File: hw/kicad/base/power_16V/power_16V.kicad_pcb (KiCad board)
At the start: 2 copper layers, 45 x 45 mm, 33 parts, among them J1 USB_B_Micro, J3 TOP, J4 BUTTOM, U1 LM2596S-5, U2 LM1117MP-3.3, U3 CP2104

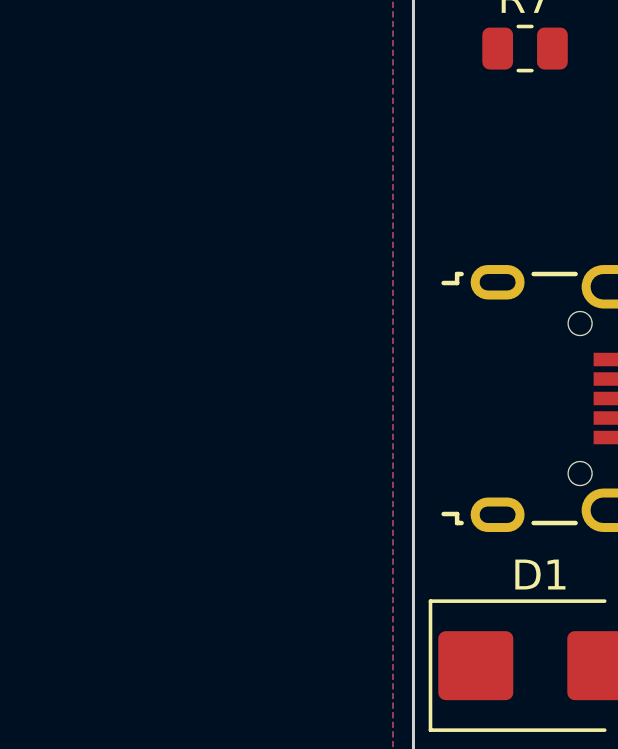
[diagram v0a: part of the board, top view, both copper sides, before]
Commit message: 增加电流传感器芯片
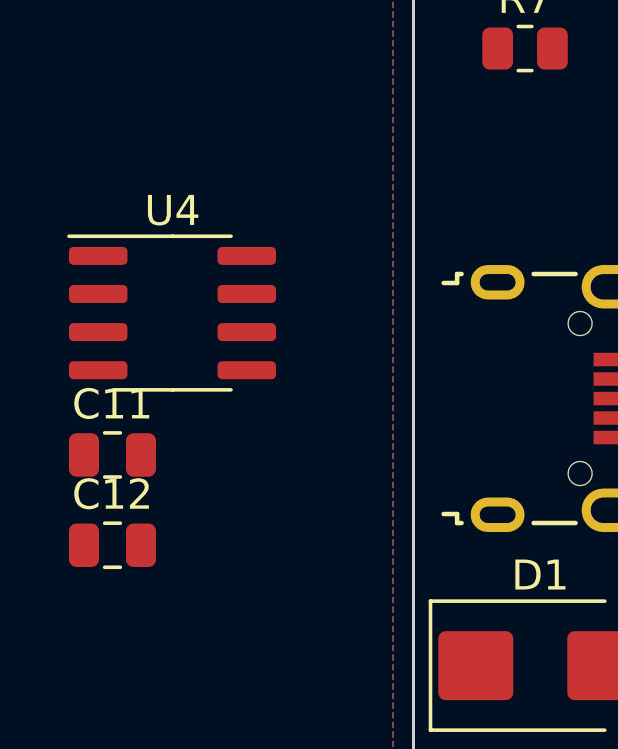
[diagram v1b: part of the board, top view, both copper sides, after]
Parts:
- added C11: 0.1uF, Capacitor_SMD:C_0805_2012Metric, F.Cu at (40.7, 61.1)
- added C12: 0.1uF, Capacitor_SMD:C_0805_2012Metric, F.Cu at (40.7, 64.1)
- added U4: ACS712xLCTR-05B, Package_SO:SOIC-8_3.9x4.9mm_P1.27mm, F.Cu at (42.7, 56.4)
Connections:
- net Net-(D6-A) renamed /DCDC_+5V
- C10 pad 1: +BATT -> Net-(J2-+)

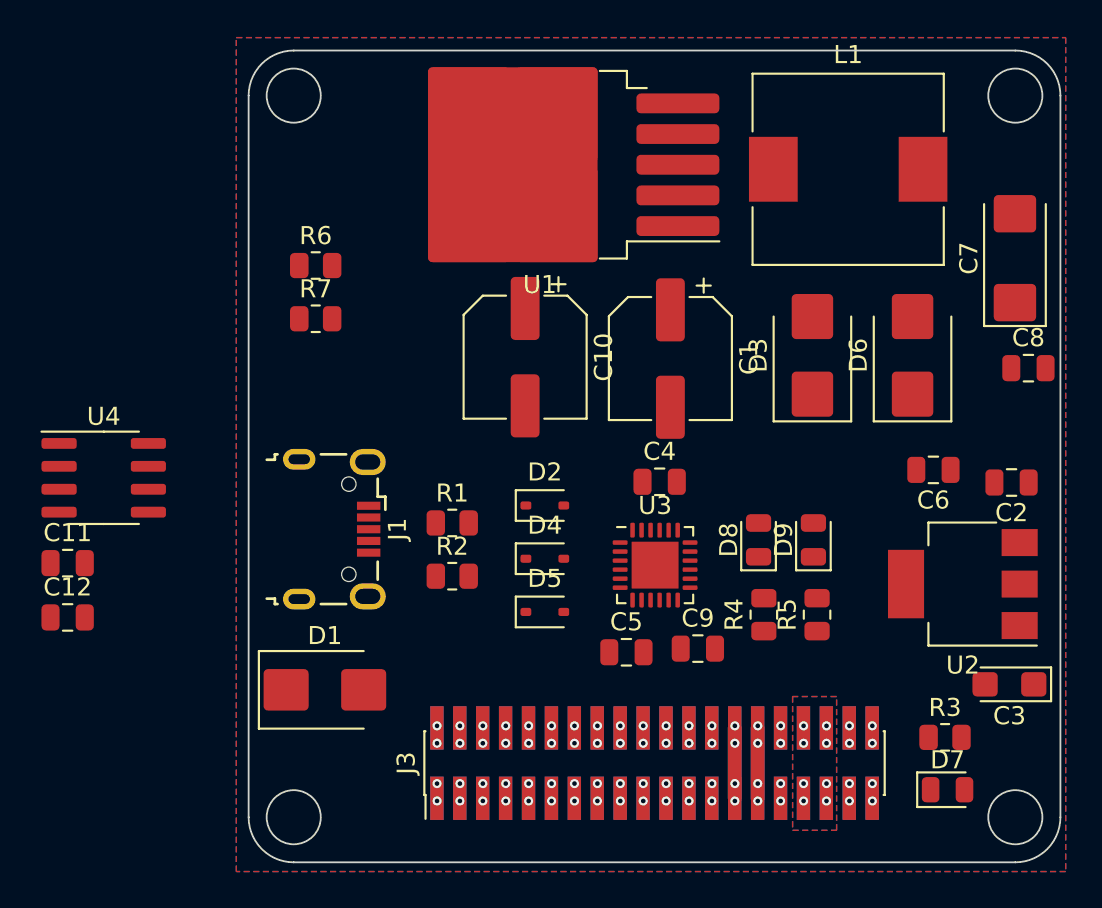
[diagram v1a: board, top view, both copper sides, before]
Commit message: 更新power16V板
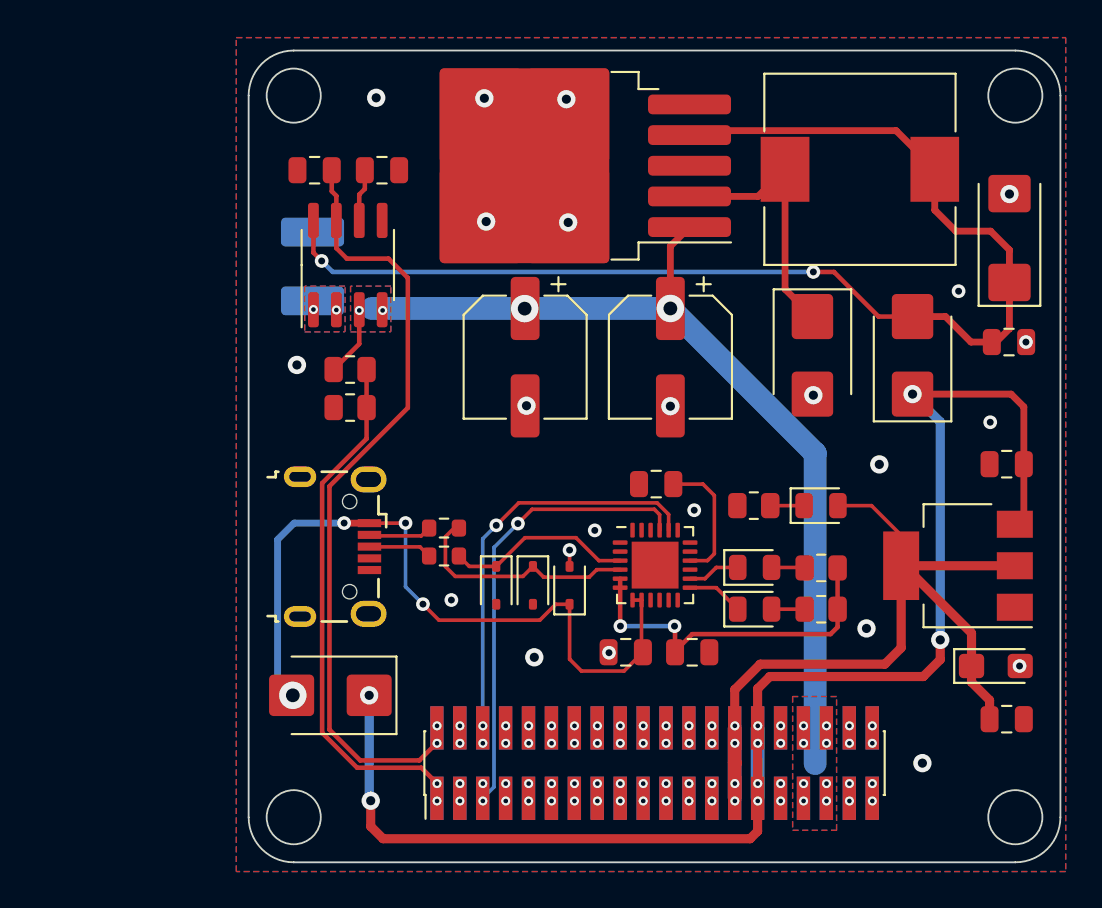
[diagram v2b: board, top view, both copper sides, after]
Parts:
- added ?: , , B.Cu at (54.3, 46.6)
- added ?: , , B.Cu at (54.3, 42.8)
- R1, R2: footprint Resistor_SMD:R_0805_2012Metric -> Resistor_SMD:R_0603_1608Metric
- R4, R5: value 22 -> 100
- moved C12 28.3 mm to (54.4, 39.4), turned to 180 degrees
- moved C11 27.9 mm to (58.1, 39.4)
- moved U4 17.9 mm to (56.2, 44.6), turned to 90 degrees
- moved D7 17.2 mm to (82.4, 57.9)
- moved R3 16.7 mm to (78.7, 57.9)
- moved C6 14.4 mm to (92.7, 69.8), turned to 0 degrees
- moved R6 6.07 mm to (56.3, 50.4)
- moved R7 5.28 mm to (56.3, 52.5), turned to 180 degrees
- moved D2 4.63 mm to (68.5, 62.4), turned to 90 degrees
- moved D8 3.85 mm to (78.8, 63.7), turned to 0 degrees
- moved D9 3.60 mm to (78.8, 61.4), turned to 0 degrees
- moved R4 3.19 mm to (82.5, 63.7), turned to 0 degrees
- moved D5 3.07 mm to (64.4, 62.4), turned to -90 degrees
- moved R2 2.71 mm to (61.6, 59.2)
- moved R5 2.60 mm to (82.5, 61.4), turned to 0 degrees
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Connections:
- C10 pad 1: Net-(J2-+) -> +BATT
- U4 pad 1: Net-(J2-+) -> /+BATT_IN
- U4 pad 2: Net-(J2-+) -> /+BATT_IN
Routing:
- net +5V: track 7.80 -> 82.5 mm, vias 4 -> 8
- net /DCDC_+5V: track 0.00 -> 69.0 mm, vias 0 -> 2
- net +BATT: track 0.00 -> 54.2 mm, vias 8 -> 12
- net /ADC_2: track 0.00 -> 43.8 mm
- net +3.3V: track 7.80 -> 49.4 mm
- net Net-(D1-A): track 0.00 -> 41.5 mm, vias 0 -> 4
- net /ADC_1: track 0.00 -> 29.5 mm
- net /UART1_Rx: track 0.00 -> 25.2 mm, vias 2 -> 3
- net /UART1_Tx: track 0.00 -> 22.8 mm, vias 2 -> 3
- net /VIO: track 0.00 -> 20.0 mm, vias 0 -> 2
- net Net-(D3-K): track 0.00 -> 14.7 mm
- net Net-(D4-K): track 0.00 -> 13.2 mm
- net Net-(D5-K): track 0.00 -> 10.4 mm
- net Net-(U3-VPP): track 0.00 -> 7.27 mm
- net Net-(J1-D+): track 0.00 -> 3.52 mm
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- added copper zone on B.Cu, net +BATT
- added copper zone on F.Cu, net +BATT
- added copper zone on B.Cu, net /+BATT_IN
- added copper zone on F.Cu, net /+BATT_IN
- added copper zone on B.Cu, net GND
- added copper zone on F.Cu, net GND
- removed copper zone on B.Cu, net (none)
- removed copper zone on F.Cu, net (none)
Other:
- board text added: "Pindar v1.2 (Base) power16v v1.2"

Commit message: 更新CPU板
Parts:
- moved ? 0.06 mm to (54.3, 46.6)
- moved ? 0.05 mm to (54.3, 42.8)

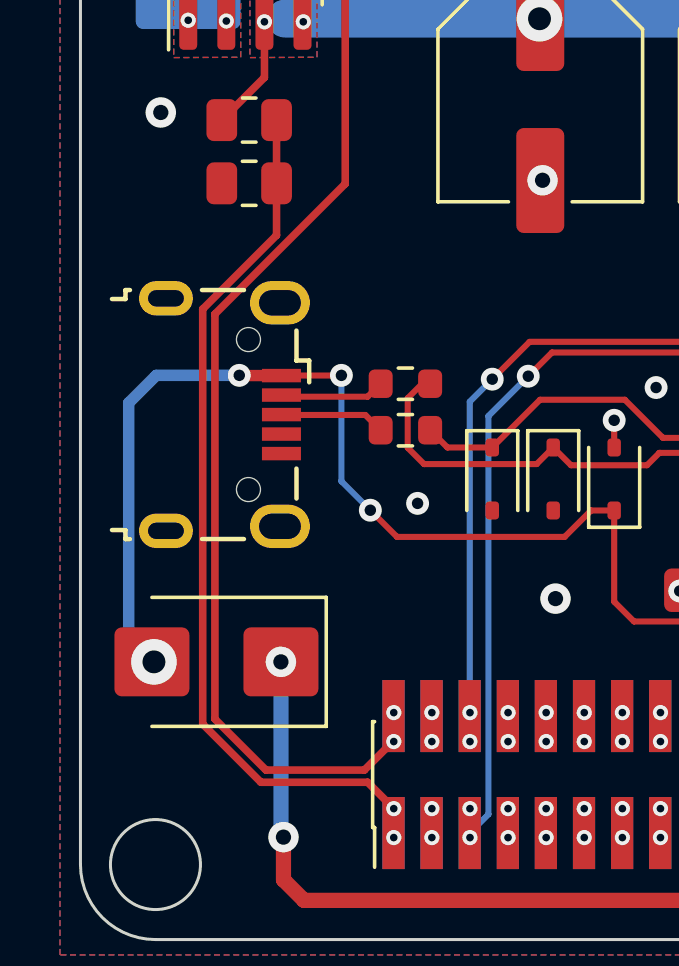
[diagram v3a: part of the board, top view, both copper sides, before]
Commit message: 更新ESP32 S3 CPU板
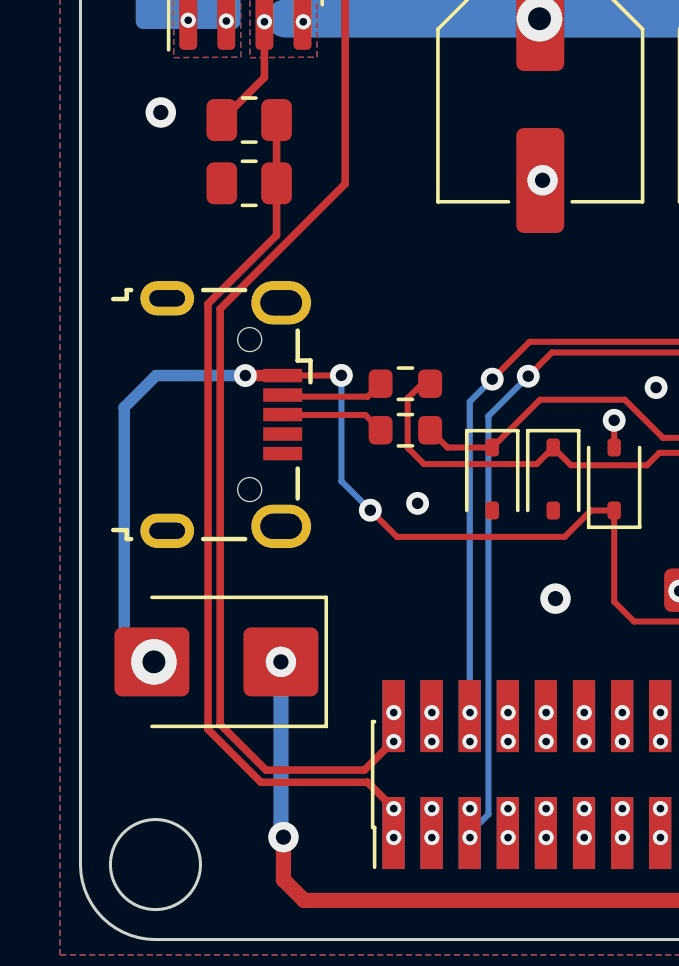
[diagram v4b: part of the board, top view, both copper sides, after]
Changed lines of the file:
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@@
   )
   (footprint "Connector_USB:USB_Micro-B_Wuerth_629105150521" (layer "F.Cu")
-    (at 55.52 60.22 -90)
+    (at 55.561 60.22 -90)
     (descr "USB Micro-B receptacle, http://www.mouser.com/ds/2/445/629105150521-469306.pdf")
     (tags "usb micro receptacle")
@@
   (via (at 75.1332 71.12) (size 0.508) (drill 0.254) (layers "F.Cu" "B.Cu") (net 13))
   (via (at 75.1332 70.1548) (size 0.508) (drill 0.254) (layers "F.Cu" "B.Cu") (net 13))
-  (segment (start 61.155 73.34) (end 60.2918 72.4768) (width 0.254) (layer "F.Cu") (net 14))
+  (segment (start 57.2567 54.2415) (end 57.2567 52.5124) (width 0.254) (layer "F.Cu") (net 14))
   (segment (start 61.155 74.17) (end 61.155 73.34) (width 0.254) (layer "F.Cu") (net 14))
   (segment (start 57.2567 50.4042) (end 57.2567 52.5124) (width 0.254) (layer "F.Cu") (net 14))
-  (segment (start 57.2567 54.2415) (end 57.2567 52.5124) (width 0.254) (layer "F.Cu") (net 14))
+  (segment (start 54.9726 70.714736) (end 54.9726 56.5256) (width 0.254) (layer "F.Cu") (net 14))
+  (segment (start 56.734664 72.4768) (end 54.9726 70.714736) (width 0.254) (layer "F.Cu") (net 14))
   (segment (start 60.2918 72.4768) (end 56.734664 72.4768) (width 0.254) (layer "F.Cu") (net 14))
-  (segment (start 54.7948 70.536936) (end 54.7948 56.7034) (width 0.254) (layer "F.Cu") (net 14))
-  (segment (start 54.7948 56.7034) (end 57.2567 54.2415) (width 0.254) (layer "F.Cu") (net 14))
-  (segment (start 56.734664 72.4768) (end 54.7948 70.536936) (width 0.254) (layer "F.Cu") (net 14))
+  (segment (start 61.155 73.34) (end 60.2918 72.4768) (width 0.254) (layer "F.Cu") (net 14))
+  (segment (start 54.9726 56.5256) (end 57.2567 54.2415) (width 0.254) (layer "F.Cu") (net 14))
   (via (at 61.1632 73.3552) (size 0.508) (drill 0.254) (layers "F.Cu" "B.Cu") (net 14))
   (via (at 61.1632 74.3204) (size 0.508) (drill 0.254) (layers "F.Cu" "B.Cu") (net 14))
@@
   (segment (start 63.695 70.27) (end 63.695 59.792) (width 0.2032) (layer "B.Cu") (net 18))
   (segment (start 63.695 59.792) (end 64.4468 59.0402) (width 0.2032) (layer "B.Cu") (net 18))
-  (segment (start 60.1846 72.0704) (end 56.903 72.0704) (width 0.254) (layer "F.Cu") (net 19))
   (segment (start 55.5822 40.7776) (end 55.3282 40.5236) (width 0.254) (layer "F.Cu") (net 19))
-  (segment (start 56.903 72.0704) (end 55.2012 70.3686) (width 0.254) (layer "F.Cu") (net 19))
-  (segment (start 55.2012 70.3686) (end 55.2012 56.871736) (width 0.254) (layer "F.Cu") (net 19))
-  (segment (start 59.5446 45.3242) (end 58.4778 44.2574) (width 0.254) (layer "F.Cu") (net 19))
-  (segment (start 55.3282 40.5236) (end 55.3282 39.3552) (width 0.254) (layer "F.Cu") (net 19))
+  (segment (start 56.903 72.0704) (end 55.379 70.5464) (width 0.254) (layer "F.Cu") (net 19))
   (segment (start 55.5822 43.6732) (end 55.5822 42.138) (width 0.254) (layer "F.Cu") (net 19))
-  (segment (start 56.1664 44.2574) (end 55.5822 43.6732) (width 0.254) (layer "F.Cu") (net 19))
+  (segment (start 61.155 71.1) (end 60.1846 72.0704) (width 0.254) (layer "F.Cu") (net 19))
   (segment (start 61.155 70.27) (end 61.155 71.1) (width 0.254) (layer "F.Cu") (net 19))
-  (segment (start 55.2012 56.871736) (end 59.5446 52.528336) (width 0.254) (layer "F.Cu") (net 19))
+  (segment (start 55.3282 40.5236) (end 55.3282 39.3552) (width 0.254) (layer "F.Cu") (net 19))
+  (segment (start 60.1846 72.0704) (end 56.903 72.0704) (width 0.254) (layer "F.Cu") (net 19))
+  (segment (start 55.379 56.693936) (end 59.5446 52.528336) (width 0.254) (layer "F.Cu") (net 19))
+  (segment (start 56.1664 44.2574) (end 55.5822 43.6732) (width 0.254) (layer "F.Cu") (net 19))
+  (segment (start 55.379 70.5464) (end 55.379 56.693936) (width 0.254) (layer "F.Cu") (net 19))
+  (segment (start 58.4778 44.2574) (end 56.1664 44.2574) (width 0.254) (layer "F.Cu") (net 19))
+  (segment (start 59.5446 45.3242) (end 58.4778 44.2574) (width 0.254) (layer "F.Cu") (net 19))
   (segment (start 55.5822 42.138) (end 55.5822 40.7776) (width 0.254) (layer "F.Cu") (net 19))
   (segment (start 59.5446 52.528336) (end 59.5446 45.3242) (width 0.254) (layer "F.Cu") (net 19))
-  (segment (start 58.4778 44.2574) (end 56.1664 44.2574) (width 0.254) (layer "F.Cu") (net 19))
-  (segment (start 61.155 71.1) (end 60.1846 72.0704) (width 0.254) (layer "F.Cu") (net 19))
   (via (at 61.1632 70.1548) (size 0.508) (drill 0.254) (layers "F.Cu" "B.Cu") (net 19))
   (via (at 61.1632 71.12) (size 0.508) (drill 0.254) (layers "F.Cu" "B.Cu") (net 19))
@@
   (segment (start 59.4176 58.9132) (end 59.4108 58.92) (width 0.2032) (layer "F.Cu") (net 32))
   (segment (start 69.1712 67.1174) (end 71.5334 67.1174) (width 0.2032) (layer "F.Cu") (net 32))
-  (segment (start 56.0208 58.92) (end 56.014 58.9132) (width 0.381) (layer "F.Cu") (net 32))
   (segment (start 67.7402 63.4176) (end 68.5108 63.4176) (width 0.2032) (layer "F.Cu") (net 32))
-  (segment (start 57.42 58.92) (end 56.0208 58.92) (width 0.381) (layer "F.Cu") (net 32))
   (segment (start 66.8598 64.298) (end 67.7402 63.4176) (width 0.2032) (layer "F.Cu") (net 32))
   (segment (start 71.5334 67.1174) (end 72.5748 66.076) (width 0.2032) (layer "F.Cu") (net 32))
   (segment (start 72.4986 63.1873) (end 72.502 63.1839) (width 0.2032) (layer "F.Cu") (net 32))
   (segment (start 60.3828 63.409) (end 61.2718 64.298) (width 0.2032) (layer "F.Cu") (net 32))
+  (segment (start 57.42 58.92) (end 56.2172 58.92) (width 0.381) (layer "F.Cu") (net 32))
   (segment (start 72.502 63.1839) (end 72.002 63.1839) (width 0.2032) (layer "F.Cu") (net 32))
   (segment (start 59.4108 58.92) (end 57.42 58.92) (width 0.2032) (layer "F.Cu") (net 32))
@@
   (via (at 59.4176 58.9132) (size 0.762) (drill 0.381) (layers "F.Cu" "B.Cu") (net 32))
   (via (at 60.3828 63.409) (size 0.762) (drill 0.381) (layers "F.Cu" "B.Cu") (net 32))
-  (via (at 56.014 58.9132) (size 0.762) (drill 0.381) (layers "F.Cu" "B.Cu") (net 32))
+  (via (at 56.2172 58.92) (size 0.762) (drill 0.381) (layers "F.Cu" "B.Cu") (net 32))
   (via (at 53.1692 68.4636) (size 1.524) (drill 0.762) (layers "F.Cu" "B.Cu") (net 32))
   (segment (start 59.4176 62.4438) (end 59.4176 58.9132) (width 0.2032) (layer "B.Cu") (net 32))
-  (segment (start 53.2454 58.9132) (end 56.014 58.9132) (width 0.381) (layer "B.Cu") (net 32))
-  (segment (start 52.3271 67.6215) (end 52.3271 59.8315) (width 0.381) (layer "B.Cu") (net 32))
+  (segment (start 53.1692 68.4636) (end 52.1786 67.473) (width 0.381) (layer "B.Cu") (net 32))
+  (segment (start 52.1786 67.473) (end 52.1786 59.98) (width 0.381) (layer "B.Cu") (net 32))
+  (segment (start 53.2386 58.92) (end 56.2172 58.92) (width 0.381) (layer "B.Cu") (net 32))
   (segment (start 60.3828 63.409) (end 59.4176 62.4438) (width 0.2032) (layer "B.Cu") (net 32))
-  (segment (start 52.3271 59.8315) (end 53.2454 58.9132) (width 0.381) (layer "B.Cu") (net 32))
-  (segment (start 53.1692 68.4636) (end 52.3271 67.6215) (width 0.381) (layer "B.Cu") (net 32))
+  (segment (start 52.1786 59.98) (end 53.2386 58.92) (width 0.381) (layer "B.Cu") (net 32))
   (segment (start 92.8948 43.7748) (end 91.8534 42.7334) (width 0.381) (layer "F.Cu") (net 33))
   (segment (start 89.923 42.7334) (end 88.7552 41.5656) (width 0.381) (layer "F.Cu") (net 33))
@@
   (segment (start 79.7076 61.3747) (end 81.5148 61.3747) (width 0.2032) (layer "F.Cu") (net 42))
   (segment (start 81.5148 61.3747) (end 81.5425 61.4024) (width 0.2032) (layer "F.Cu") (net 42))
-  (segment (start 57.42 59.57) (end 57.4744 59.6244) (width 0.2032) (layer "F.Cu") (net 43))
   (segment (start 60.2944 59.6244) (end 60.7262 59.1926) (width 0.2032) (layer "F.Cu") (net 43))
   (segment (start 57.4744 59.6244) (end 60.2944 59.6244) (width 0.2032) (layer "F.Cu") (net 43))
   (segment (start 57.434 60.234) (end 60.2182 60.234) (width 0.2032) (layer "F.Cu") (net 44))
   (segment (start 60.2182 60.234) (end 60.7262 60.742) (width 0.2032) (layer "F.Cu") (net 44))
-  (segment (start 57.42 60.22) (end 57.434 60.234) (width 0.2032) (layer "F.Cu") (net 44))
   (via (at 54.3122 47.0768) (size 0.508) (drill 0.254) (layers "F.Cu" "B.Cu") (net 58))
   (via (at 55.5822 47.1022) (size 0.508) (drill 0.254) (layers "F.Cu" "B.Cu") (net 58))
